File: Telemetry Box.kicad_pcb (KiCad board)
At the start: 4 copper layers, 82 parts, among them J1 USB_C_Receptacle, J2 DC 5V In, J3 Conn_01x06, J4 Thermistor Molex, J5 Micro_SD_Card, J6 Thermistor Molex, J8 SMA, Q1 MMBT2222A-TP, SW2 SW_Push, U1 AP2112K-1.8, U10 MAX-M10S, U2 TPS62160DSG, U3 STM32F373CCTx, U4 LSM6DSRXTR, U5 MCP6L01x-xLT, U7 BMP585, U8 MCP6L01x-xLT, U9 USBLC6-2P6, X1 32.768kHz

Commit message: Updated Schematics & finished rev2 layout. Routing left
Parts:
- C1, C2, C21, C26, C27, C32, C33: moved to B.Cu
- moved C33 75.7 mm to (126.1, 120.3), turned to 180 degrees
- moved C32 61.6 mm to (140.5, 121.5), turned to 90 degrees
- moved D2 61.4 mm to (148.4, 110.0), turned to -90 degrees
- moved D4 60.7 mm to (151.7, 110.0), turned to -90 degrees
- moved D1 58.5 mm to (150.1, 110.0), turned to -90 degrees
- moved R41 56.6 mm to (148.5, 113.2), turned to -90 degrees
- moved R44 56.2 mm to (151.7, 113.2), turned to -90 degrees
- moved C20 56.0 mm to (146.9, 113.2), turned to -90 degrees
- moved C6 55.7 mm to (141.6, 116.6), turned to 90 degrees
- moved R40 54.1 mm to (150.1, 113.2), turned to -90 degrees
- moved R15 53.6 mm to (148.3, 122.8), turned to 180 degrees
- moved C11 52.9 mm to (138.4, 130.1), turned to -90 degrees
- moved R43 52.4 mm to (154.4, 113.7)
- moved C10 52.0 mm to (136.9, 130.1), turned to -90 degrees
- moved C8 51.9 mm to (136.2, 127.3), turned to 180 degrees
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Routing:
- net /MCU/Crystal_1: track 0.95 -> 0.00 mm

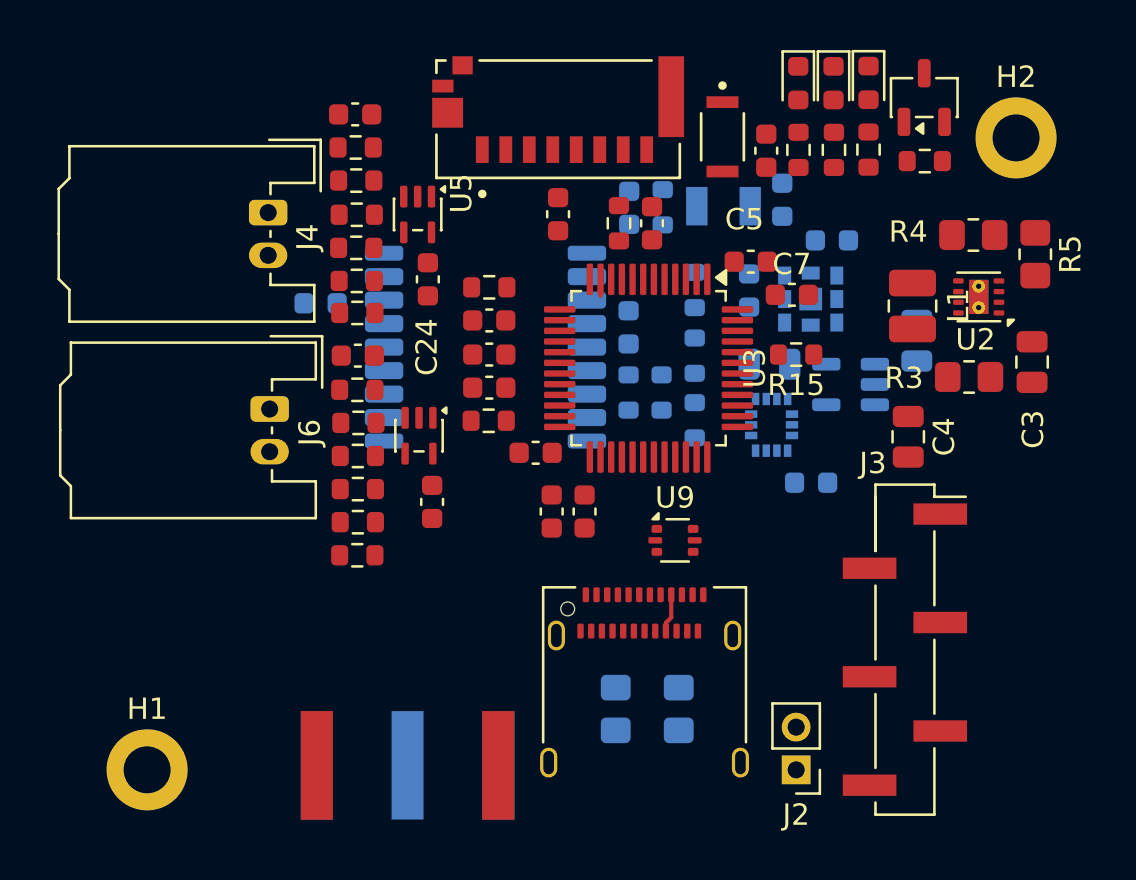
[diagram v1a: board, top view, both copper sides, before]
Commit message: Moved buck & LDO to shrink board
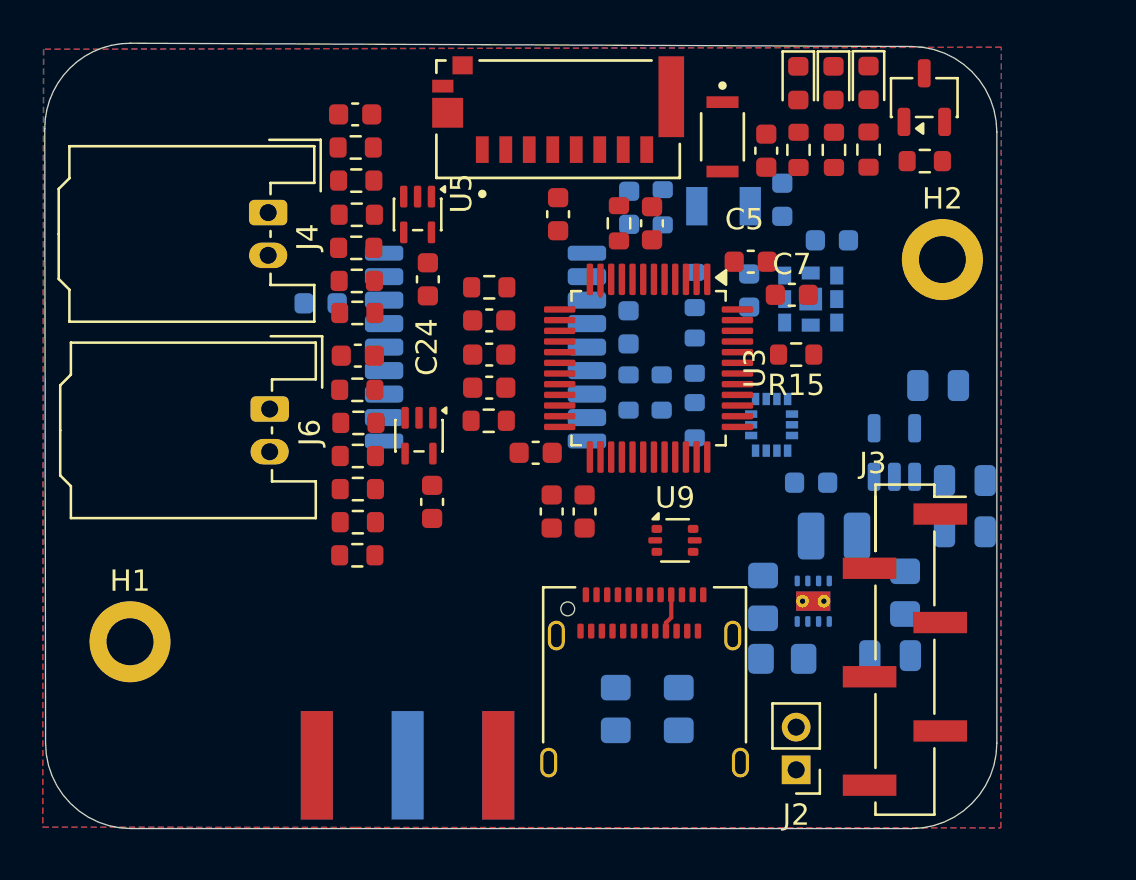
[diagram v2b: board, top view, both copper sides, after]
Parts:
- C3, C4, L1, R3, R4, R5, U2: moved to B.Cu
- moved R5 22.4 mm to (147.7, 137.0), turned to 0 degrees
- moved R4 19.6 mm to (146.8, 134.1), turned to -90 degrees
- moved U2 16.2 mm to (149.2, 134.3), turned to 90 degrees
- moved C3 15.3 mm to (152.8, 136.8), turned to 0 degrees
- moved L1 11.4 mm to (150.1, 131.2), turned to 0 degrees
- moved R3 10.5 mm to (153.4, 133.9), turned to 90 degrees
- moved C2 7.96 mm to (155.0, 124.2), turned to 0 degrees
- moved C1 6.93 mm to (156.2, 128.7), turned to 0 degrees
- moved H2 6.66 mm to (155.2, 118.3)
- moved H1 6.05 mm to (117.2, 136.2)
- moved C4 5.18 mm to (156.2, 131.1), turned to 0 degrees
- moved U1 3.79 mm to (152.9, 127.3), turned to 90 degrees
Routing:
- added copper zone on B.Cu, net PGND
- added copper zone on F.Cu, net PGND
- added copper zone on In1.Cu, net PGND
- added copper zone on In2.Cu, net PGND
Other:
- board outline added: 44.6 x 36.8 mm
